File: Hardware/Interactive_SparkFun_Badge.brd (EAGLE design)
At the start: 68.5 x 102.6 mm, 31 parts, among them J1 AVR_SPI_PRG_6NS, U1 ATMEGA328P, Y1 8MHZ

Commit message: moving oscillator
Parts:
- moved Y1 9.44 mm to (16.5, 37.5)
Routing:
- net N$2: track 11.0 -> 2.95 mm
- net N$3: track 11.4 -> 3.52 mm
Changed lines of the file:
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@@
 <attribute name="PROD_ID" value="RES-00824" x="-53.34" y="31.115" size="1.778" layer="27" rot="R270" display="off"/>
 </element>
-<element name="Y1" library="SparkFun-FreqCtrl" package="RESONATOR-SMD" value="8MHZ" x="10.16" y="30.48">
-<attribute name="PROD_ID" value="XTAL-08895" x="50.8" y="-30.48" size="1.778" layer="27" display="off"/>
+<element name="Y1" library="SparkFun-FreqCtrl" package="RESONATOR-SMD" value="8MHZ" x="16.51" y="37.465">
+<attribute name="PROD_ID" value="XTAL-08895" x="57.15" y="-23.495" size="1.778" layer="27" display="off"/>
 </element>
 <element name="C1" library="SparkFun-Capacitors" package="EIA3216" value="10uF" x="29.21" y="30.48" rot="R180">
@@
 <contactref element="U1" pad="7"/>
 <contactref element="Y1" pad="1"/>
-<wire x1="14.7" y1="40.1574" x2="14.7" y2="37.56" width="0.254" layer="1"/>
-<wire x1="14.7" y1="37.56" x2="8.96" y2="31.82" width="0.254" layer="1"/>
-<wire x1="8.96" y1="31.496" x2="8.96" y2="31.82" width="0.254" layer="1"/>
+<wire x1="14.7" y1="40.1574" x2="14.7" y2="39.275" width="0.254" layer="1"/>
+<wire x1="14.7" y1="39.275" x2="15.24" y2="38.735" width="0.254" layer="1"/>
+<wire x1="15.24" y1="38.735" x2="15.24" y2="37.535" width="0.254" layer="1"/>
+<wire x1="15.24" y1="37.535" x2="15.31" y2="37.465" width="0.254" layer="1"/>
 </signal>
 <signal name="N$3">
 <contactref element="U1" pad="8"/>
 <contactref element="Y1" pad="3"/>
-<wire x1="15.5" y1="40.1574" x2="15.5" y2="36.455" width="0.254" layer="1"/>
-<wire x1="15.5" y1="36.455" x2="11.43" y2="32.385" width="0.254" layer="1"/>
-<wire x1="11.43" y1="32.385" x2="11.43" y2="30.55" width="0.254" layer="1"/>
-<wire x1="11.43" y1="30.55" x2="11.36" y2="30.48" width="0.254" layer="1"/>
+<wire x1="15.5" y1="40.1574" x2="15.5" y2="39.11" width="0.254" layer="1"/>
+<wire x1="15.5" y1="39.11" x2="15.875" y2="38.735" width="0.254" layer="1"/>
+<wire x1="15.875" y1="38.735" x2="17.456" y2="38.735" width="0.254" layer="1"/>
+<wire x1="17.456" y1="38.735" x2="17.71" y2="38.481" width="0.254" layer="1"/>
 </signal>
 <signal name="GND">
@@
 <contactref element="U1" pad="20"/>
 <contactref element="C4" pad="1"/>
-<wire x1="13.1" y1="48.7426" x2="13.1" y2="50.4" width="0.254" layer="1"/>
-<wire x1="13.1" y1="50.4" x2="11.43" y2="52.07" width="0.254" layer="1"/>
-<wire x1="11.43" y1="52.07" x2="10.795" y2="52.07" width="0.254" layer="1"/>
-<wire x1="10.795" y1="52.07" x2="10.16" y2="52.705" width="0.254" layer="1"/>
-<wire x1="10.16" y1="52.705" x2="10.16" y2="53.125" width="0.254" layer="1"/>
+<wire x1="13.1" y1="48.7426" x2="13.1" y2="49.765" width="0.254" layer="1"/>
+<wire x1="13.1" y1="49.765" x2="10.795" y2="52.07" width="0.254" layer="1"/>
+<wire x1="10.795" y1="52.07" x2="10.795" y2="52.49" width="0.254" layer="1"/>
+<wire x1="10.795" y1="52.49" x2="10.16" y2="53.125" width="0.254" layer="1"/>
 </signal>
 <signal name="N$5">

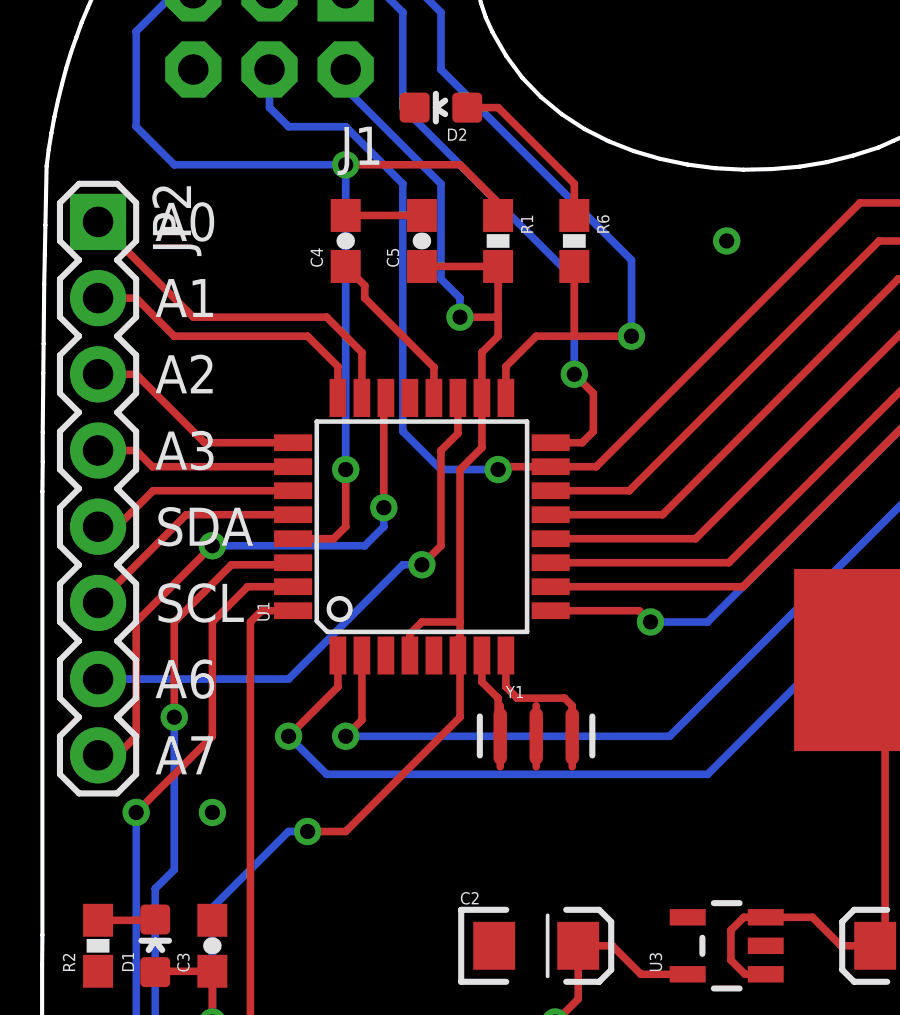
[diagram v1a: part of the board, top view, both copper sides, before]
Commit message: Updating line widths
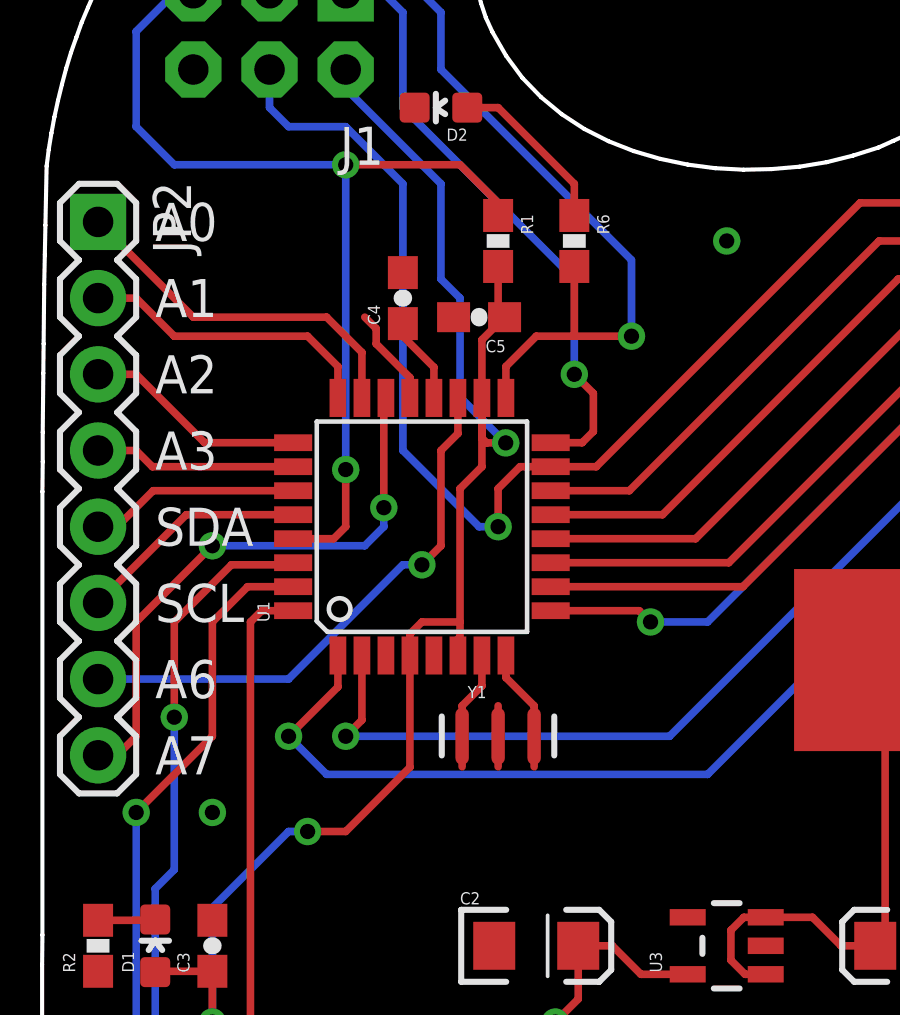
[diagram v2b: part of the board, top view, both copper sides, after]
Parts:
- moved C5 3.18 mm to (14.6, 51.4), turned to 180 degrees
- moved C4 2.69 mm to (12.1, 52.1)
- moved Y1 1.27 mm to (15.2, 37.5)
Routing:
- net VCC: track 81.5 -> 84.2 mm
- net N$8: track 5.60 -> 2.91 mm
- net MOSI: track 51.5 -> 54.2 mm
- net N$3: track 3.52 -> 2.07 mm
- net N$2: track 2.95 -> 1.95 mm
- net GND: track 5.17 -> 5.94 mm
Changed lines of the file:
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@@
 <attribute name="PROD_ID" value="RES-00824" x="-53.34" y="31.115" size="1.778" layer="27" rot="R270" display="off"/>
 </element>
-<element name="Y1" library="SparkFun-FreqCtrl" package="RESONATOR-SMD" value="8MHZ" x="16.51" y="37.465">
-<attribute name="PROD_ID" value="XTAL-08895" x="57.15" y="-23.495" size="1.778" layer="27" display="off"/>
+<element name="Y1" library="SparkFun-FreqCtrl" package="RESONATOR-SMD" value="8MHZ" x="15.24" y="37.465">
+<attribute name="PROD_ID" value="XTAL-08895" x="55.88" y="-23.495" size="1.778" layer="27" display="off"/>
 </element>
 <element name="C1" library="SparkFun-Capacitors" package="EIA3216" value="10uF" x="29.21" y="30.48" rot="R180">
@@
 <attribute name="PROD_ID" value="CAP-00810" x="66.675" y="95.25" size="1.778" layer="27" rot="R90" display="off"/>
 </element>
-<element name="C4" library="SparkFun-Capacitors" package="0603-CAP" value="0.1uF" x="10.16" y="53.975" rot="R90">
-<attribute name="PROD_ID" value="CAP-00810" x="78.74" y="69.215" size="1.778" layer="27" rot="R90" display="off"/>
-</element>
-<element name="C5" library="SparkFun-Capacitors" package="0603-CAP" value="0.1uF" x="12.7" y="53.975" rot="R90">
-<attribute name="PROD_ID" value="CAP-00810" x="81.28" y="73.025" size="1.778" layer="27" rot="R90" display="off"/>
+<element name="C4" library="SparkFun-Capacitors" package="0603-CAP" value="0.1uF" x="12.065" y="52.07" rot="R90">
+<attribute name="PROD_ID" value="CAP-00810" x="80.645" y="67.31" size="1.778" layer="27" rot="R90" display="off"/>
+</element>
+<element name="C5" library="SparkFun-Capacitors" package="0603-CAP" value="0.1uF" x="14.605" y="51.435" rot="R180">
+<attribute name="PROD_ID" value="CAP-00810" x="-4.445" y="120.015" size="1.778" layer="27" rot="R180" display="off"/>
 </element>
 <element name="R2" library="SparkFun-Resistors" package="0603-RES" value="10K" x="1.905" y="30.48" rot="R90">
@@
 <contactref element="U1" pad="7"/>
 <contactref element="Y1" pad="1"/>
-<wire x1="14.7" y1="40.1574" x2="14.7" y2="39.275" width="0.254" layer="1"/>
-<wire x1="14.7" y1="39.275" x2="15.24" y2="38.735" width="0.254" layer="1"/>
-<wire x1="15.24" y1="38.735" x2="15.24" y2="37.535" width="0.254" layer="1"/>
-<wire x1="15.24" y1="37.535" x2="15.31" y2="37.465" width="0.254" layer="1"/>
+<wire x1="14.7" y1="40.1574" x2="14.7" y2="39.141" width="0.254" layer="1"/>
+<wire x1="14.7" y1="39.141" x2="14.04" y2="38.481" width="0.254" layer="1"/>
 </signal>
 <signal name="N$3">
 <contactref element="U1" pad="8"/>
 <contactref element="Y1" pad="3"/>
-<wire x1="15.5" y1="40.1574" x2="15.5" y2="39.11" width="0.254" layer="1"/>
-<wire x1="15.5" y1="39.11" x2="15.875" y2="38.735" width="0.254" layer="1"/>
-<wire x1="15.875" y1="38.735" x2="17.456" y2="38.735" width="0.254" layer="1"/>
-<wire x1="17.456" y1="38.735" x2="17.71" y2="38.481" width="0.254" layer="1"/>
+<wire x1="15.5" y1="40.1574" x2="15.5" y2="39.421" width="0.254" layer="1"/>
+<wire x1="15.5" y1="39.421" x2="16.44" y2="38.481" width="0.254" layer="1"/>
 </signal>
 <signal name="GND">
@@
 <contactref element="D2" pad="C"/>
 <contactref element="J1" pad="6"/>
-<wire x1="10.16" y1="54.825" x2="12.7" y2="54.825" width="0.254" layer="1"/>
 <polygon width="0.254" layer="16" isolate="0.3048">
 <vertex x="-5.08" y="100.33"/>
@@
 <via x="22.86" y="53.975" extent="1-16" drill="0.508"/>
 <via x="5.715" y="34.925" extent="1-16" drill="0.508"/>
+<wire x1="12.3" y1="48.7426" x2="12.3" y2="49.422" width="0.254" layer="1"/>
+<wire x1="12.3" y1="49.422" x2="11.176" y2="50.546" width="0.254" layer="1"/>
+<wire x1="11.176" y1="50.546" x2="11.176" y2="51.054" width="0.254" layer="1"/>
+<wire x1="11.176" y1="51.054" x2="10.795" y2="51.435" width="0.254" layer="1"/>
 </signal>
 <signal name="VCC">
@@
 <wire x1="3.175" y1="17.78" x2="5.715" y2="20.32" width="0.254" layer="16"/>
 <wire x1="5.715" y1="20.32" x2="5.715" y2="27.94" width="0.254" layer="16"/>
-<wire x1="12.7" y1="53.125" x2="15.24" y2="53.125" width="0.254" layer="1"/>
 <via x="8.89" y="34.29" extent="1-16" drill="0.508"/>
 <wire x1="8.89" y1="34.29" x2="8.255" y2="34.29" width="0.254" layer="16"/>
@@
 <wire x1="10.16" y1="34.29" x2="8.89" y2="34.29" width="0.254" layer="1"/>
 <wire x1="13.97" y1="40.0874" x2="13.9" y2="40.1574" width="0.254" layer="1"/>
-<wire x1="13.97" y1="40.0874" x2="13.97" y2="38.1" width="0.254" layer="1"/>
-<wire x1="13.97" y1="38.1" x2="10.16" y2="34.29" width="0.254" layer="1"/>
-<wire x1="14.7" y1="48.7426" x2="14.7" y2="47.085" width="0.254" layer="1"/>
-<wire x1="14.7" y1="47.085" x2="13.97" y2="46.355" width="0.254" layer="1"/>
-<wire x1="13.97" y1="46.355" x2="13.97" y2="41.275" width="0.254" layer="1"/>
+<wire x1="13.97" y1="40.0874" x2="13.97" y2="38.1" width="0" layer="19" extent="1-16"/>
+<wire x1="14.7" y1="48.7426" x2="14.7" y2="46.45" width="0.254" layer="1"/>
+<wire x1="13.97" y1="45.72" x2="13.97" y2="41.275" width="0.254" layer="1"/>
 <wire x1="10.16" y1="59.69" x2="10.16" y2="59.055" width="0.254" layer="16"/>
 <wire x1="10.16" y1="59.055" x2="13.335" y2="55.88" width="0.254" layer="16"/>
-<via x="13.97" y="51.435" extent="1-16" drill="0.508"/>
-<wire x1="14.7" y1="48.7426" x2="14.7" y2="50.26" width="0.254" layer="1"/>
-<wire x1="14.7" y1="50.26" x2="15.24" y2="50.8" width="0.254" layer="1"/>
-<wire x1="15.24" y1="50.8" x2="15.24" y2="51.435" width="0.254" layer="1"/>
-<wire x1="15.24" y1="51.435" x2="15.24" y2="53.125" width="0.254" layer="1"/>
-<wire x1="13.97" y1="51.435" x2="15.24" y2="51.435" width="0.254" layer="1"/>
+<via x="15.494" y="47.244" extent="1-16" drill="0.508"/>
 <wire x1="13.335" y1="55.88" x2="13.335" y2="52.705" width="0.254" layer="16"/>
 <wire x1="13.335" y1="52.705" x2="13.97" y2="52.07" width="0.254" layer="16"/>
-<wire x1="13.97" y1="52.07" x2="13.97" y2="51.435" width="0.254" layer="16"/>
+<wire x1="13.97" y1="52.07" x2="13.97" y2="48.768" width="0.254" layer="16"/>
+<wire x1="13.97" y1="48.768" x2="15.494" y2="47.244" width="0.254" layer="16"/>
+<wire x1="14.7" y1="48.7426" x2="14.7" y2="50.68" width="0.254" layer="1"/>
+<wire x1="14.7" y1="50.68" x2="15.455" y2="51.435" width="0.254" layer="1"/>
+<wire x1="15.494" y1="47.244" x2="14.859" y2="47.244" width="0.254" layer="1"/>
+<wire x1="14.7" y1="46.45" x2="13.97" y2="45.72" width="0.254" layer="1"/>
+<wire x1="14.7" y1="48.7426" x2="14.7" y2="47.403" width="0.254" layer="1"/>
+<wire x1="14.7" y1="47.403" x2="14.859" y2="47.244" width="0.254" layer="1"/>
+<wire x1="15.24" y1="53.125" x2="15.24" y2="51.65" width="0.254" layer="1"/>
+<wire x1="15.24" y1="51.65" x2="15.455" y2="51.435" width="0.254" layer="1"/>
+<wire x1="10.16" y1="34.29" x2="12.3" y2="36.43" width="0.254" layer="1"/>
+<wire x1="12.3" y1="40.1574" x2="12.3" y2="36.43" width="0.254" layer="1"/>
 </signal>
 <signal name="RXI">
@@
 <contactref element="C4" pad="1"/>
 <wire x1="13.1" y1="48.7426" x2="13.1" y2="49.765" width="0.254" layer="1"/>
-<wire x1="13.1" y1="49.765" x2="10.795" y2="52.07" width="0.254" layer="1"/>
-<wire x1="10.795" y1="52.07" x2="10.795" y2="52.49" width="0.254" layer="1"/>
-<wire x1="10.795" y1="52.49" x2="10.16" y2="53.125" width="0.254" layer="1"/>
+<wire x1="13.1" y1="49.765" x2="12.065" y2="50.8" width="0.254" layer="1"/>
+<wire x1="12.065" y1="50.8" x2="12.065" y2="51.22" width="0.254" layer="1"/>
 </signal>
 <signal name="N$5">
@@
 <wire x1="16.9926" y1="46.45" x2="18.51" y2="46.45" width="0.254" layer="1"/>
 <wire x1="18.51" y1="46.45" x2="27.305" y2="55.245" width="0.254" layer="1"/>
-<via x="15.24" y="46.355" extent="1-16" drill="0.508"/>
-<wire x1="15.24" y1="46.355" x2="13.335" y2="46.355" width="0.254" layer="16"/>
-<wire x1="13.335" y1="46.355" x2="12.065" y2="47.625" width="0.254" layer="16"/>
-<wire x1="12.065" y1="47.625" x2="12.065" y2="55.88" width="0.254" layer="16"/>
+<via x="15.24" y="44.45" extent="1-16" drill="0.508"/>
+<wire x1="12.065" y1="46.99" x2="12.065" y2="55.88" width="0.254" layer="16"/>
 <wire x1="12.065" y1="55.88" x2="10.16" y2="57.785" width="0.254" layer="16"/>
 <wire x1="10.16" y1="57.785" x2="8.255" y2="57.785" width="0.254" layer="16"/>
 <wire x1="8.255" y1="57.785" x2="7.62" y2="58.42" width="0.254" layer="16"/>
 <wire x1="7.62" y1="58.42" x2="7.62" y2="59.69" width="0.254" layer="16"/>
-<wire x1="16.9926" y1="46.45" x2="15.335" y2="46.45" width="0.254" layer="1"/>
-<wire x1="15.335" y1="46.45" x2="15.24" y2="46.355" width="0.254" layer="1"/>
+<wire x1="16.9926" y1="46.45" x2="15.97" y2="46.45" width="0.254" layer="1"/>
+<wire x1="15.97" y1="46.45" x2="15.24" y2="45.72" width="0.254" layer="1"/>
+<wire x1="15.24" y1="45.72" x2="15.24" y2="44.45" width="0.254" layer="1"/>
+<wire x1="12.065" y1="46.99" x2="14.605" y2="44.45" width="0.254" layer="16"/>
+<wire x1="14.605" y1="44.45" x2="15.24" y2="44.45" width="0.254" layer="16"/>
 </signal>
 <signal name="MISO">

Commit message: New board design
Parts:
- removed STANDOFF1: STAND-OFF, SparkFun-Electromechanical:STAND-OFF
- removed U$2: FLAME, Local Library:FLAME
- LOGO1: value OSHW-LOGOM -> OSHW-LOGOL; device SparkFun-Aesthetics:OSHW-LOGO-M -> SparkFun-Aesthetics:OSHW-LOGO-L
- LOGO2: value SFE_LOGO_NAME.1_INCH -> SFE_LOGO_NAME_FLAME.3_INCH; device SparkFun-Aesthetics:SFE_LOGO_NAME_.1 -> SparkFun-Aesthetics:SFE_LOGO_NAME_FLAME_.3
- moved J1 82.0 mm to (86.4, 38.1), turned to 270 degrees
- moved LOGO1 67.6 mm to (62.9, 36.2)
- moved JP3 58.3 mm to (41.9, 1.27), turned to 0 degrees
- moved R1 55.3 mm to (46.4, 8.26), turned to 0 degrees
- moved LOGO2 55.2 mm to (1.27, 40.6)
- moved C5 55.1 mm to (46.4, 6.35)
- moved JP2 53.5 mm to (5.71, 1.27), turned to 0 degrees
- moved BAT1 42.5 mm to (76.8, 17.8), turned to 270 degrees
- moved U1 42.3 mm to (44.5, 16.5), turned to 180 degrees
- moved D2 41.8 mm to (38.1, 24.8), turned to 0 degrees
- moved C4 41.7 mm to (34.9, 17.1), turned to 180 degrees
- moved Y1 41.5 mm to (52.1, 18.4), turned to 90 degrees
- moved R6 38.8 mm to (38.1, 21.0)
- moved R3 36.1 mm to (52.7, 51.4), turned to 0 degrees
- moved FID2 35.3 mm to (86.4, 61.0)
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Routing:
- net VCC: track 84.2 -> 139.5 mm, vias 4 -> 3
- net D3: track 68.7 -> 18.2 mm, vias 1 -> 0
- net D4: track 66.6 -> 18.2 mm, vias 1 -> 0
- net RAW: track 17.4 -> 58.8 mm, vias 0 -> 2
- net MISO: track 20.3 -> 59.5 mm, vias 1 -> 2
- net D9: track 48.5 -> 14.5 mm
- net A0: track 12.1 -> 46.1 mm, vias 0 -> 3
- net SCK: track 29.3 -> 60.8 mm, vias 1 -> 2
- net TXO: track 23.2 -> 54.5 mm
- net A1: track 9.99 -> 40.8 mm
- net A2: track 7.45 -> 38.2 mm
- net RESET: track 33.1 -> 63.2 mm
- net A3: track 6.73 -> 36.8 mm
- net D10: track 39.6 -> 9.54 mm
- net SDA: track 7.00 -> 34.9 mm
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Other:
- board size 68.5 x 102.6 mm -> 88.9 x 63.5 mm

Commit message: Updating with engineering review changes
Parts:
- removed C1, C2: 10uF, SparkFun-Capacitors:EIA3216
- removed C3: 0.1uF, SparkFun-Capacitors:0603-CAP
- removed U3: (no value), SparkFun-PowerIC:SOT23-5
- added D3, D4: MBRA140, SparkFun-DiscreteSemi:SMA-DIODE
- JP3: device SparkFun-Connectors:1X06_LOCK -> SparkFun-Connectors:1X06
- moved SG1 19.4 mm to (11.2, 13.4)
- moved C5 11.0 mm to (51.1, 16.2), turned to 0 degrees
- moved D2 4.07 mm to (34.9, 22.2), turned to 270 degrees
- moved R6 3.24 mm to (34.9, 20.3), turned to 0 degrees
- moved C4 1.80 mm to (36.2, 15.9)
- moved Y1 1.42 mm to (51.4, 19.7)
- moved R1 1.27 mm to (46.4, 6.99)
- moved D1 0.74 mm to (24.1, 19.3), turned to 270 degrees
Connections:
- removed net RAW: BAT1.1, C1.A, U3.1, U3.3
- new net 3.3V: D3.A, JP1.VCC
- new net N$10: BAT1.1, D4.A
- net D3: now also JP3.DTR; no longer JP3.1
- net D4: now also JP3.RXI; no longer JP3.2
- net D5: now also JP3.TXO; no longer JP3.3
- net D6: now also JP3.VCC; no longer JP3.4
- net D7: now also JP3.CTS; no longer JP3.5
- net D8: now also JP3.GND; no longer JP3.6
- net GND: no longer C1.C, C2.C, C3.2, U3.2
- net VCC: now also D3.C, D4.C; no longer C2.A, C3.1, JP1.VCC, U3.5
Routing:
- net RAW: track 58.8 -> 0.00 mm, vias 2 -> 0
- net VCC: track 139.5 -> 119.9 mm
- net N$10: track 0.00 -> 13.4 mm
- net D2: track 48.7 -> 35.9 mm
- net D8: track 46.6 -> 39.7 mm
- net D7: track 43.7 -> 36.8 mm
- net 3.3V: track 0.00 -> 6.11 mm
- net RESET: track 63.2 -> 69.0 mm
- net D6: track 40.8 -> 35.4 mm
- net D5: track 30.0 -> 34.3 mm
- net GND: track 0.00 -> 3.46 mm, vias 6 -> 2
- net SCK: track 60.8 -> 62.9 mm
- net D3: track 18.2 -> 19.7 mm
- net N$5: track 3.89 -> 2.49 mm
- net N$2: track 2.95 -> 1.69 mm
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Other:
- outline, holes or cut-outs redrawn
- board text added: "A4"
- board text added: "A5"
- board text removed: "SCL"
- board text removed: "SDA"
